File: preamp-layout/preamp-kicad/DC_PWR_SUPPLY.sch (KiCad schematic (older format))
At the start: 24 parts, among them J10 Conn_01x02_Male, J3 Conn_01x04_Male, J4 Conn_01x02_Female, J7 Screw_Terminal_01x03, J8 Conn_01x04_Male, J9 Conn_01x02_Male, K1 G5RLU-1A-E

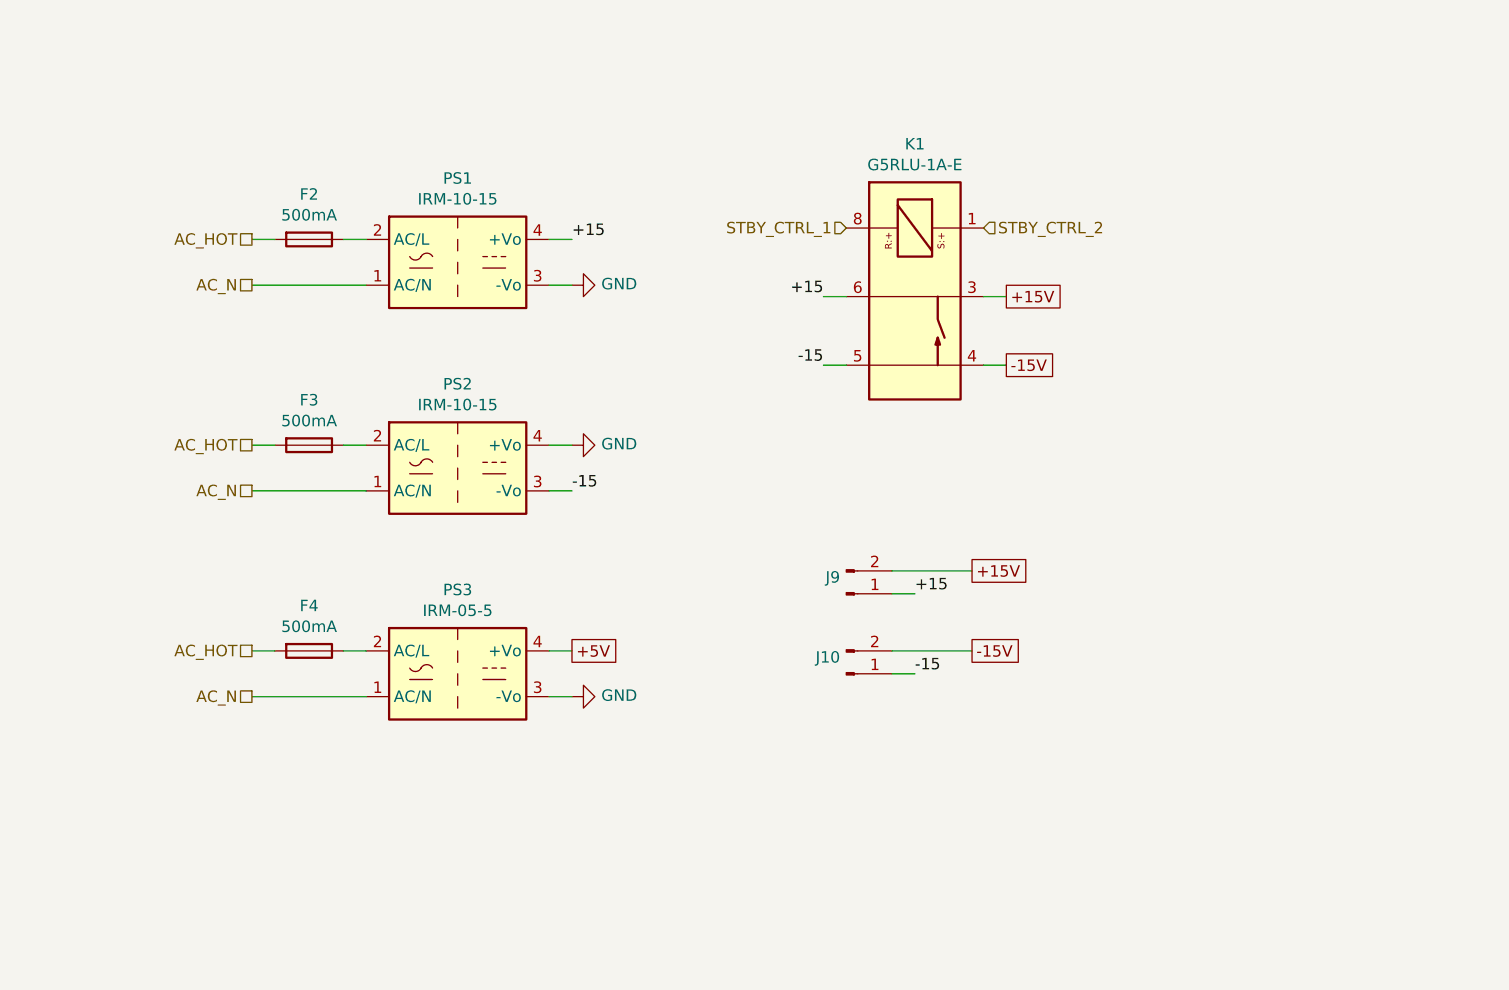
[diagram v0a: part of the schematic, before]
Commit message: Power supply filter Implementation
Added pi filter on output of DC supplies. PCB layout update on the power supply board.
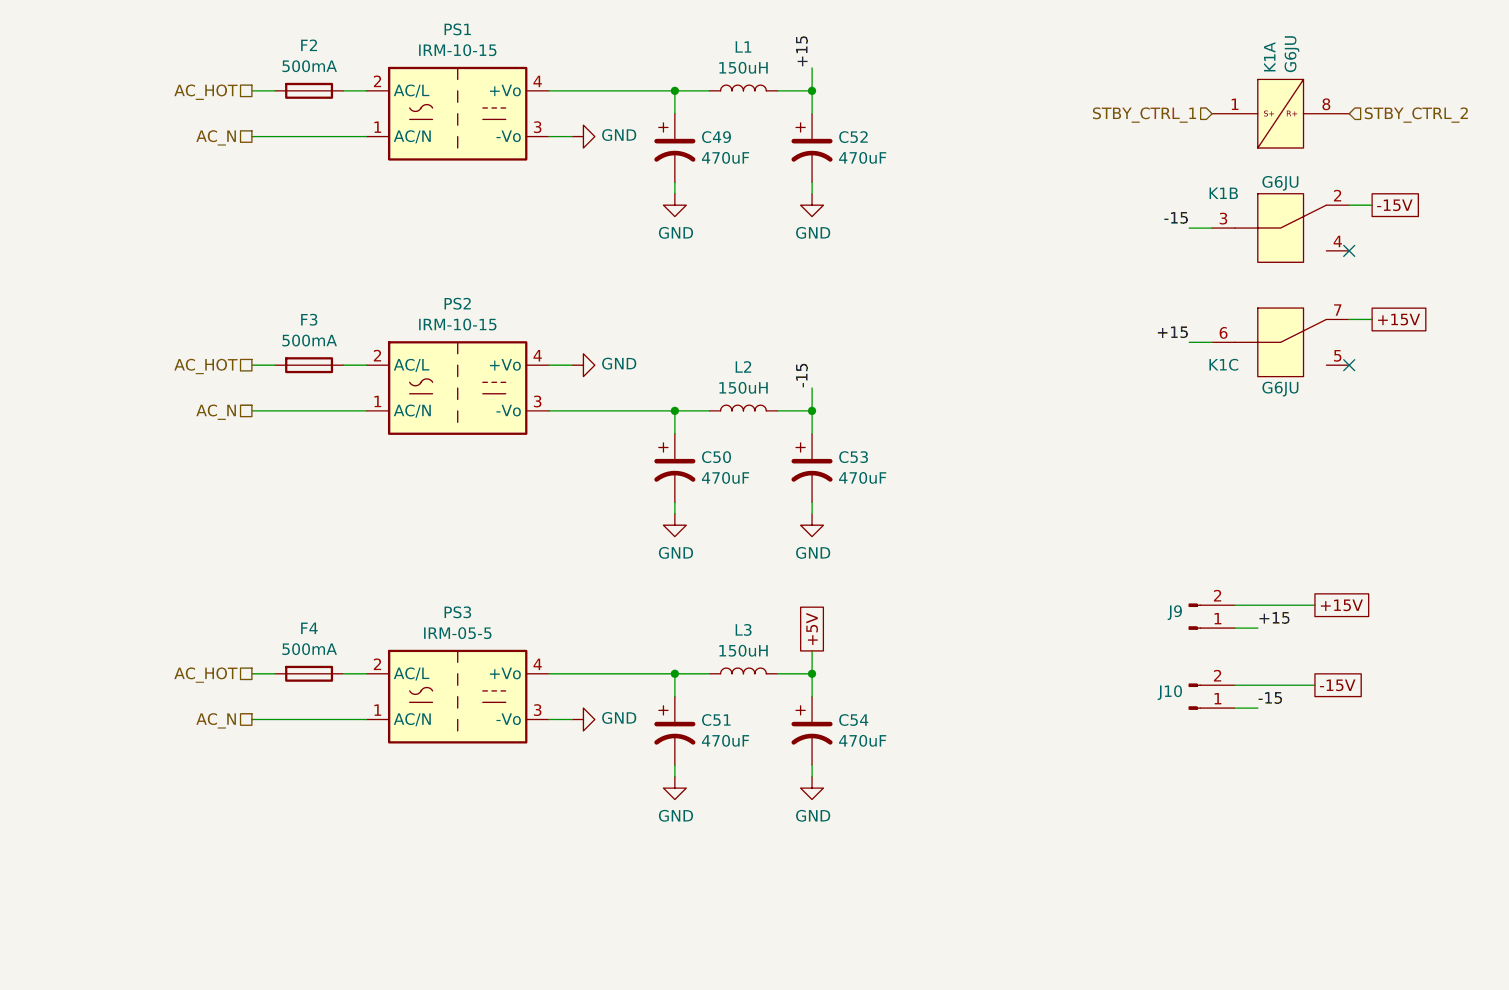
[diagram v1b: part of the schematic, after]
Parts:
- removed K1: G5RLU-1A-E, symbol preamp:G5RLU-1A-E
- added C49, C50, C51, C52, C53, C54: 470uF, Capacitor_THT:CP_Radial_D12.5mm_P5.00mm, symbol Device:CP1
- added K1: G6JU, preamp:Relay_DPDT_Omron_G6JU-2P-Y, symbol preamp:G6JU
- added L1, L2, L3: 150uH, Inductor_THT:L_Axial_L23.4mm_D12.7mm_P7.62mm_Vertical_Vishay_IHA-203, symbol Device:L
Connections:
- net +15: now also C52.1, K1.6, L1.2; no longer PS1.4 (+Vo)
- net +15V: now also K1.7
- net +5V: now also C54.1, L3.2; no longer PS3.4 (+Vo)
- net -15: now also C53.1, K1.3, L2.2; no longer PS2.3 (-Vo)
- net -15V: now also K1.2
- net GND: now also C49.2, C50.2, C51.2, C52.2, C53.2, C54.2
- net STBY_CTRL_1: now also K1.1
- net STBY_CTRL_2: now also K1.8
- new net: C49.1, L1.1, PS1.4 (+Vo)
- new net: C50.1, L2.1, PS2.3 (-Vo)
- new net: C51.1, L3.1, PS3.4 (+Vo)
- no-connect marks 0 -> 2
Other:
- moved on the sheet: F2, F3, F4, J10, J9, PS1, PS2, PS3

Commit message: many changes made, too long ago to remember
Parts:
- added D63, D64: RED, LED_SMD:LED_1206_3216Metric_Pad1.42x1.75mm_HandSolder, symbol Device:LED
- added R118, R139: 330R, Resistor_SMD:R_1206_3216Metric_Pad1.42x1.75mm_HandSolder, symbol Device:R
- added R146, R147: 51R, Resistor_SMD:R_1206_3216Metric_Pad1.42x1.75mm_HandSolder, symbol Device:R
- added TP45, TP46, TP47, TP48: TestPoint, TestPoint:TestPoint_Pad_D2.0mm, symbol Connector:TestPoint
- added U12: ULN2003, Package_SO:SOIC-16_3.9x9.9mm_P1.27mm, symbol Transistor_Array:ULN2003
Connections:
- net +15V: now also TP45.1
- net +5V: now also R118.1, R139.1, R146.1, R147.1, TP47.1, U12.9 (COM)
- net -15V: now also TP46.1
- net GND: now also TP48.1, U12.8 (GND)
- net STBY_CTRL_1: now also D63.1 (K), R146.2, U12.16 (O1); no longer J4.1 (Pin_1)
- net STBY_CTRL_2: now also D64.1 (K), R147.2, U12.15 (O2); no longer J4.2 (Pin_2)
- new net: D63.2 (A), R118.2
- new net: D64.2 (A), R139.2
- new net STBY_RST: J4.2 (Pin_2), U12.2 (I2)
- new net STBY_SET: J4.1 (Pin_1), U12.1 (I1)
- no-connect marks 2 -> 12
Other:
- moved on the sheet: C49, C50, C51, C52, C53, C54, D2, D3, D8, F2, F3, F4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
